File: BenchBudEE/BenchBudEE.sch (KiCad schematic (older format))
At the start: 0 parts

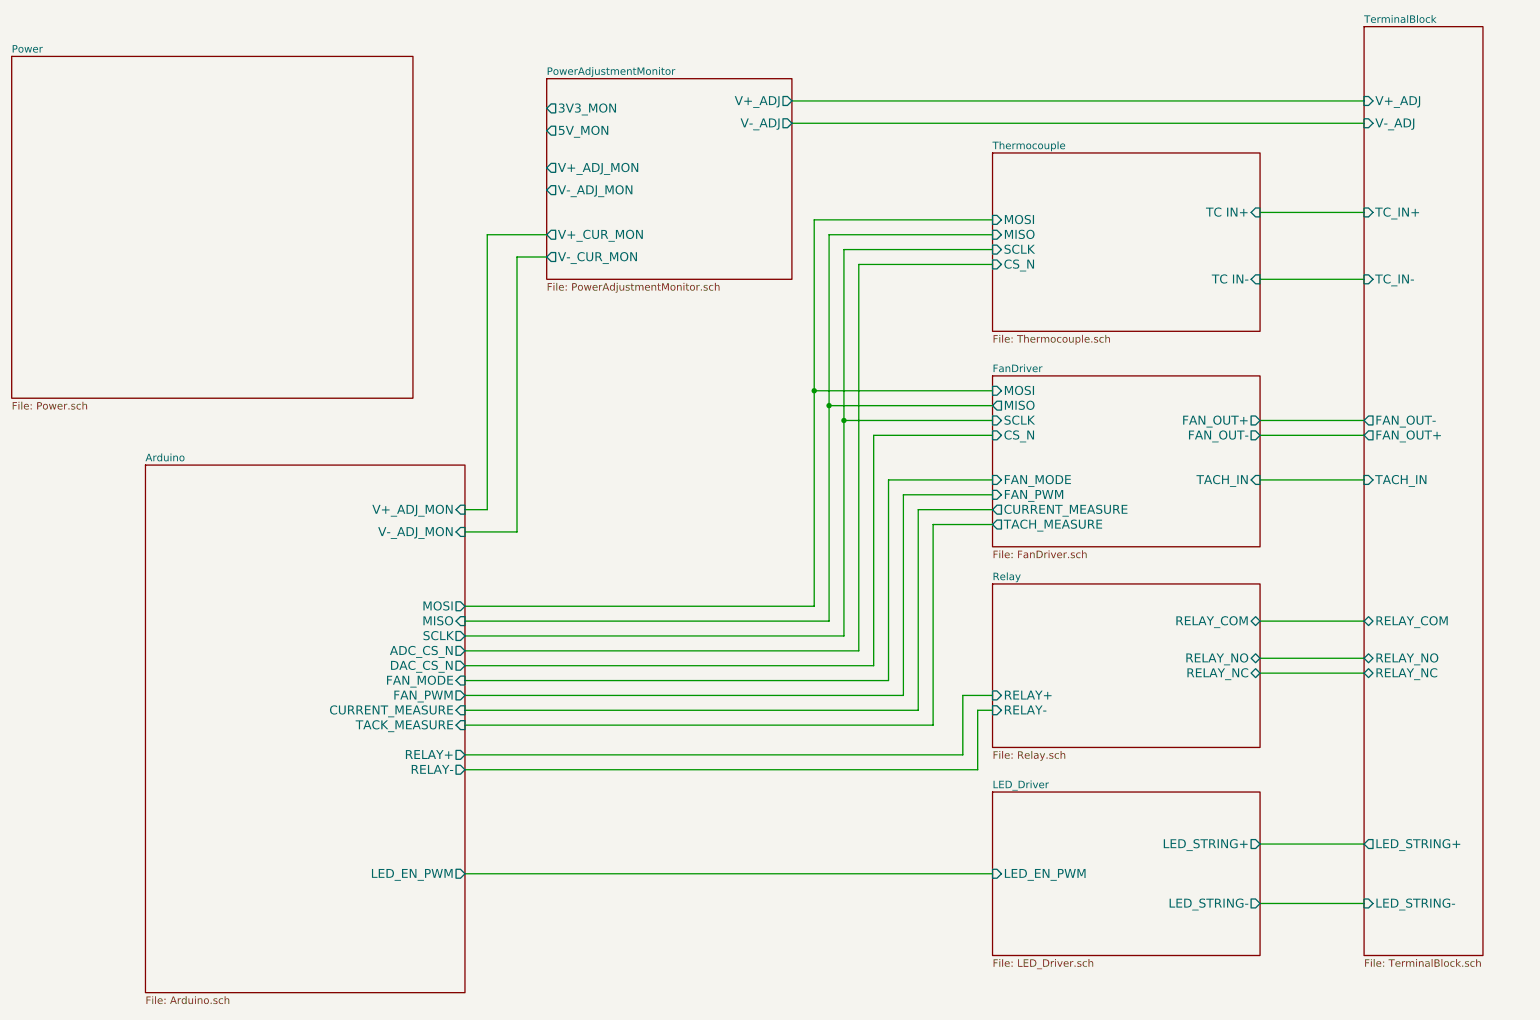
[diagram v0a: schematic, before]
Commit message: Arduino module associated + roughly placed.
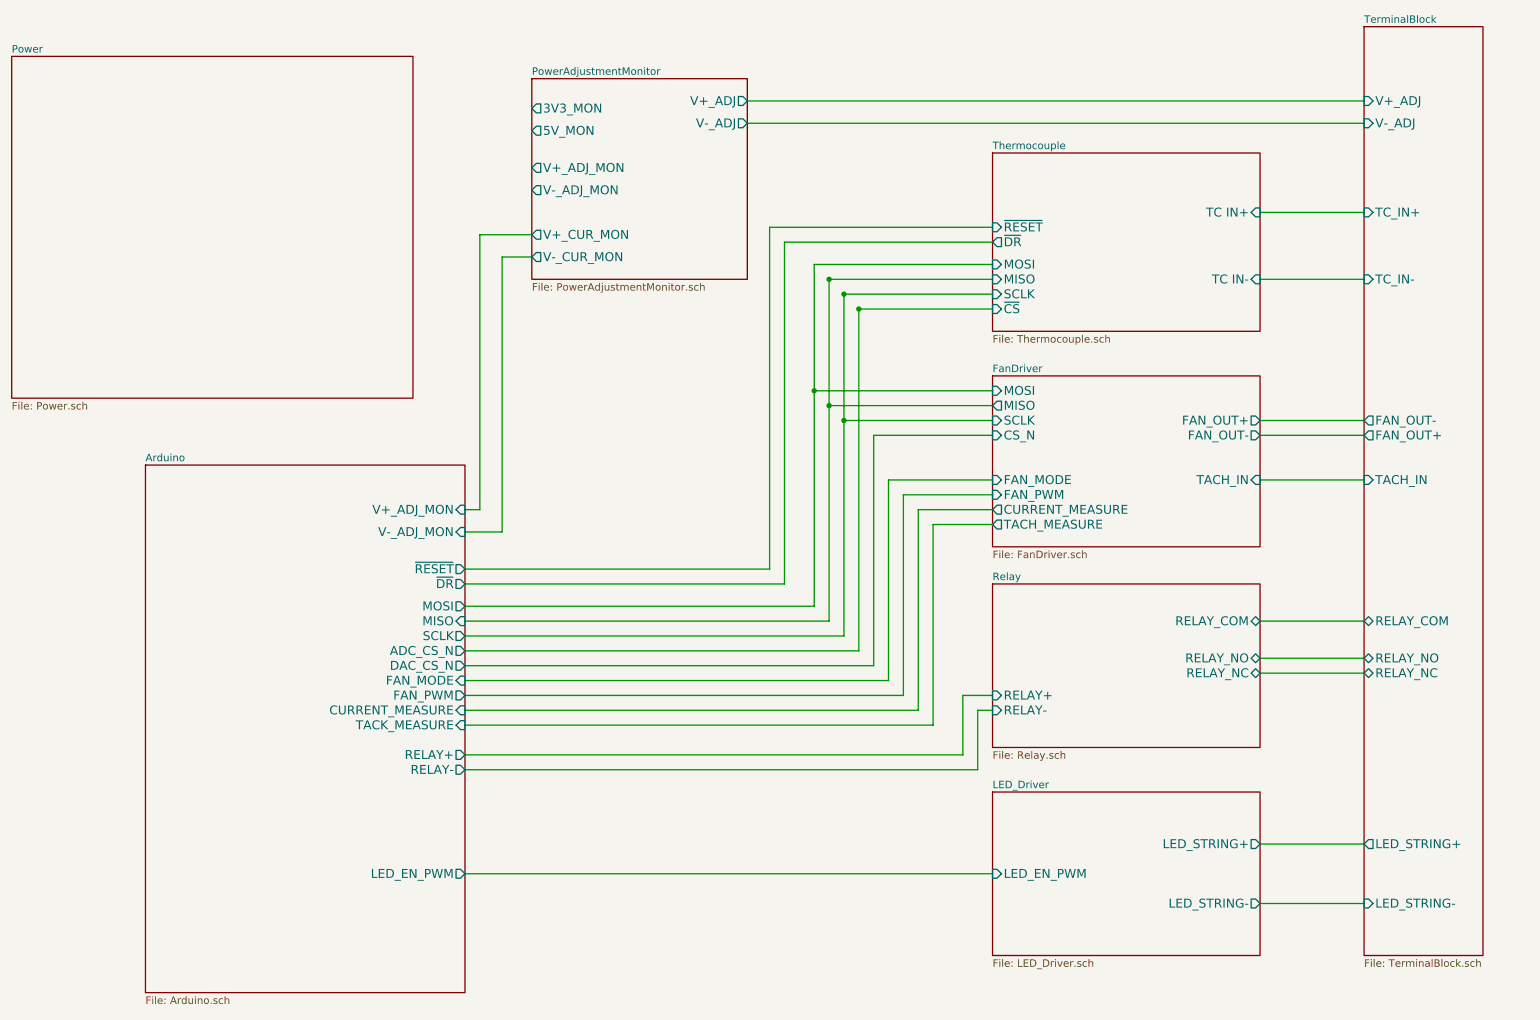
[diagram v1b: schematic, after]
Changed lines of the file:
@@
 Sheet 1 9
 Title ""
-Date "20 feb 2014"
+Date "23 feb 2014"
 Rev ""
 Comp ""
@@
 F2 "TC IN+" I R 9250 1900 60
 F3 "TC IN-" I R 9250 2350 60
-F4 "MISO" I L 7450 2050 60
-F5 "MOSI" I L 7450 1950 60
-F6 "SCLK" I L 7450 2150 60
-F7 "CS_N" I L 7450 2250 60
-$EndSheet
-$Sheet
-S 4450 1000 1650 1350
+F4 "MISO" I L 7450 2350 60
+F5 "MOSI" I L 7450 2250 60
+F6 "SCLK" I L 7450 2450 60
+F7 "~CS" I L 7450 2550 60
+F8 "~DR" O L 7450 2100 60
+F9 "~RESET" I L 7450 2000 60
+$EndSheet
+$Sheet
+S 4350 1000 1450 1350
 U 52F2C572
 F0 "PowerAdjustmentMonitor" 50
 F1 "PowerAdjustmentMonitor.sch" 50
-F2 "V+_ADJ" O R 6100 1150 60
-F3 "V-_ADJ" O R 6100 1300 60
-F4 "3V3_MON" O L 4450 1200 60
-F5 "5V_MON" O L 4450 1350 60
-F6 "V+_ADJ_MON" O L 4450 1600 60
-F7 "V-_ADJ_MON" O L 4450 1750 60
-F8 "V+_CUR_MON" O L 4450 2050 60
-F9 "V-_CUR_MON" O L 4450 2200 60
-$EndSheet
-Wire Wire Line
-	6100 1300 9950 1300
-Wire Wire Line
-	6100 1150 9950 1150
-Wire Wire Line
-	9250 3300 9950 3300
-Wire Wire Line
-	9950 3400 9250 3400
-Wire Wire Line
-	9250 3700 9950 3700
-Wire Wire Line
-	9250 2350 9950 2350
-Wire Wire Line
-	9950 1900 9250 1900
-Wire Wire Line
-	9250 5000 9950 5000
-Wire Wire Line
-	9950 4900 9250 4900
-Wire Wire Line
-	9250 4650 9950 4650
-Wire Wire Line
-	9250 6150 9950 6150
-Wire Wire Line
-	9250 6550 9950 6550
-Wire Wire Line
-	3900 3900 4050 3900
-Wire Wire Line
-	4050 3900 4050 2050
-Wire Wire Line
-	4050 2050 4450 2050
-Wire Wire Line
-	4450 2200 4250 2200
-Wire Wire Line
-	4250 2200 4250 4050
-Wire Wire Line
-	4250 4050 3900 4050
-Wire Wire Line
-	6250 1950 6250 4550
-Wire Wire Line
-	6250 1950 7450 1950
-Wire Wire Line
-	6350 2050 6350 4650
-Wire Wire Line
-	6450 2150 6450 4750
-Wire Wire Line
-	6550 2250 6550 4850
-Wire Wire Line
-	7450 3100 6250 3100
-Connection ~ 6250 3100
-Wire Wire Line
-	7450 3200 6350 3200
-Connection ~ 6350 3200
-Wire Wire Line
-	7450 3300 6450 3300
-Connection ~ 6450 3300
-Wire Wire Line
-	6950 5250 6950 3900
-Wire Wire Line
-	6950 3900 7450 3900
-Wire Wire Line
-	7450 4000 7050 4000
-Wire Wire Line
-	7050 4000 7050 5350
-Wire Wire Line
-	7450 3400 6650 3400
-Wire Wire Line
-	6650 3400 6650 4950
-Wire Wire Line
-	6550 4850 3900 4850
-Wire Wire Line
-	6650 4950 3900 4950
-Wire Wire Line
-	6250 4550 3900 4550
-Wire Wire Line
-	7450 2050 6350 2050
-Wire Wire Line
-	6450 2150 7450 2150
-Wire Wire Line
-	7450 2250 6550 2250
-Wire Wire Line
-	6350 4650 3900 4650
-Wire Wire Line
-	6450 4750 3900 4750
-Wire Wire Line
-	7450 3800 6850 3800
-Wire Wire Line
-	6850 3800 6850 5150
-Wire Wire Line
-	6850 5150 3900 5150
-Wire Wire Line
-	6950 5250 3900 5250
-Wire Wire Line
-	7050 5350 3900 5350
+F2 "V+_ADJ" O R 5800 1150 60
+F3 "V-_ADJ" O R 5800 1300 60
+F4 "3V3_MON" O L 4350 1200 60
+F5 "5V_MON" O L 4350 1350 60
+F6 "V+_ADJ_MON" O L 4350 1600 60
+F7 "V-_ADJ_MON" O L 4350 1750 60
+F8 "V+_CUR_MON" O L 4350 2050 60
+F9 "V-_CUR_MON" O L 4350 2200 60
+$EndSheet
 $Sheet
 S 1750 3600 2150 3550
@@
 F14 "FAN_PWM" O R 3900 5150 60
 F15 "FAN_MODE" I R 3900 5050 60
-$EndSheet
+F16 "~DR" O R 3900 4400 60
+F17 "~RESET" O R 3900 4300 60
+$EndSheet
+Wire Wire Line
+	6750 3700 7450 3700
+Wire Wire Line
+	6750 5050 6750 3700
+Wire Wire Line
+	3900 5050 6750 5050
+Wire Wire Line
+	3900 6350 7450 6350
+Wire Wire Line
+	7350 5650 3900 5650
+Wire Wire Line
+	7350 5250 7350 5650
+Wire Wire Line
+	7450 5250 7350 5250
+Wire Wire Line
+	7250 5150 7450 5150
+Wire Wire Line
+	7250 5550 7250 5150
 Wire Wire Line
 	3900 5550 7250 5550
 Wire Wire Line
-	7250 5550 7250 5150
-Wire Wire Line
-	7250 5150 7450 5150
-Wire Wire Line
-	7450 5250 7350 5250
-Wire Wire Line
-	7350 5250 7350 5650
-Wire Wire Line
-	7350 5650 3900 5650
-Wire Wire Line
-	3900 6350 7450 6350
-Wire Wire Line
-	3900 5050 6750 5050
-Wire Wire Line
-	6750 5050 6750 3700
-Wire Wire Line
-	6750 3700 7450 3700
+	7050 5350 3900 5350
+Wire Wire Line
+	6950 5250 3900 5250
+Wire Wire Line
+	6850 5150 3900 5150
+Wire Wire Line
+	6850 3800 6850 5150
+Wire Wire Line
+	7450 3800 6850 3800
+Wire Wire Line
+	6450 4750 3900 4750
+Wire Wire Line
+	6350 4650 3900 4650
+Wire Wire Line
+	6250 4550 3900 4550
+Wire Wire Line
+	6650 4950 3900 4950
+Wire Wire Line
+	6550 4850 3900 4850
+Wire Wire Line
+	6650 3400 6650 4950
+Wire Wire Line
+	7450 3400 6650 3400
+Wire Wire Line
+	7050 4000 7050 5350
+Wire Wire Line
+	7450 4000 7050 4000
+Wire Wire Line
+	6950 3900 7450 3900
+Wire Wire Line
+	6950 5250 6950 3900
+Connection ~ 6450 3300
+Wire Wire Line
+	7450 3300 6450 3300
+Connection ~ 6350 3200
+Wire Wire Line
+	7450 3200 6350 3200
+Connection ~ 6250 3100
+Wire Wire Line
+	7450 3100 6250 3100
+Wire Wire Line
+	6250 2250 6250 4550
+Wire Wire Line
+	4150 4050 3900 4050
+Wire Wire Line
+	4150 2200 4150 4050
+Wire Wire Line
+	4350 2200 4150 2200
+Wire Wire Line
+	4000 2050 4350 2050
+Wire Wire Line
+	4000 3900 4000 2050
+Wire Wire Line
+	3900 3900 4000 3900
+Wire Wire Line
+	9250 6550 9950 6550
+Wire Wire Line
+	9250 6150 9950 6150
+Wire Wire Line
+	9250 4650 9950 4650
+Wire Wire Line
+	9950 4900 9250 4900
+Wire Wire Line
+	9250 5000 9950 5000
+Wire Wire Line
+	9950 1900 9250 1900
+Wire Wire Line
+	9250 2350 9950 2350
+Wire Wire Line
+	9250 3700 9950 3700
+Wire Wire Line
+	9950 3400 9250 3400
+Wire Wire Line
+	9250 3300 9950 3300
+Wire Wire Line
+	5800 1150 9950 1150
+Wire Wire Line
+	5800 1300 9950 1300
+Wire Wire Line
+	7450 2550 6550 2550
+Connection ~ 6550 2550
+Wire Wire Line
+	6550 2550 6550 4850
+Wire Wire Line
+	7450 2450 6450 2450
+Connection ~ 6450 2450
+Wire Wire Line
+	6450 2450 6450 4750
+Wire Wire Line
+	7450 2350 6350 2350
+Connection ~ 6350 2350
+Wire Wire Line
+	6350 2350 6350 4650
+Wire Wire Line
+	6250 2250 7450 2250
+Wire Wire Line
+	7450 2100 6050 2100
+Wire Wire Line
+	6050 2100 6050 4400
+Wire Wire Line
+	6050 4400 3900 4400
+Wire Wire Line
+	3900 4300 5950 4300
+Wire Wire Line
+	5950 4300 5950 2000
+Wire Wire Line
+	5950 2000 7450 2000
 $EndSCHEMATC

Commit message: Fan/Current driver associated + roughly placed.
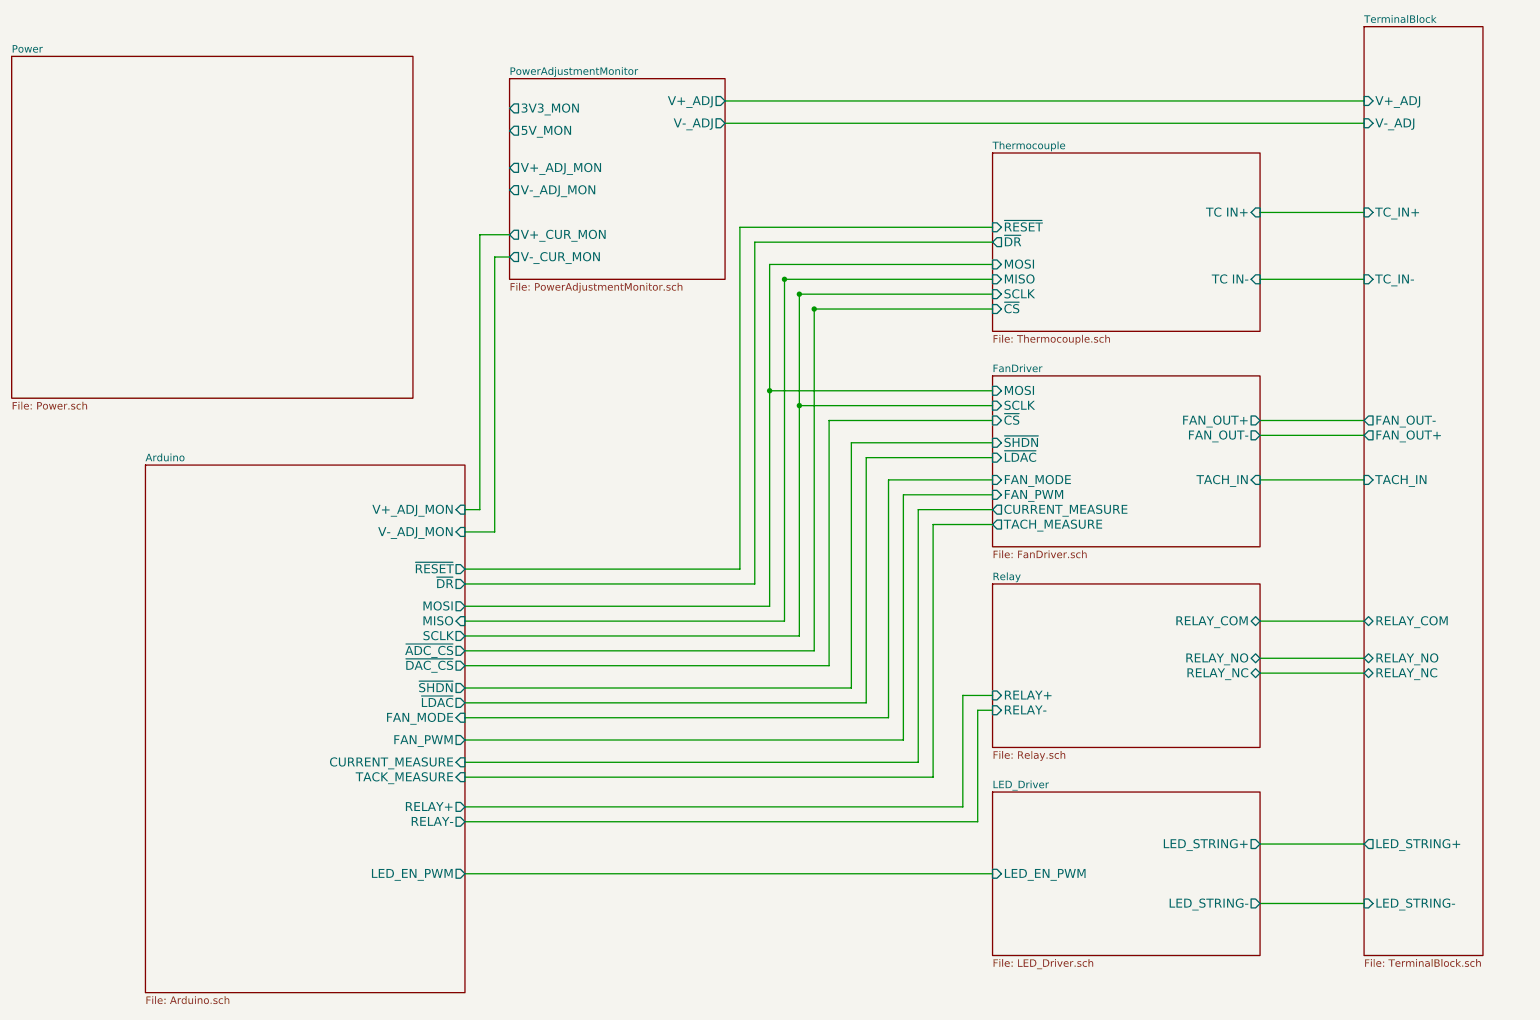
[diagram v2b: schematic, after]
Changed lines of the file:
@@
-$EndSheet
-$Sheet
-S 7450 3000 1800 1150
-U 52F1416D
-F0 "FanDriver" 50
-F1 "FanDriver.sch" 50
-F2 "CURRENT_MEASURE" O L 7450 3900 60
-F3 "MOSI" I L 7450 3100 60
-F4 "MISO" O L 7450 3200 60
-F5 "SCLK" I L 7450 3300 60
-F6 "CS_N" I L 7450 3400 60
-F7 "TACH_IN" I R 9250 3700 60
-F8 "TACH_MEASURE" O L 7450 4000 60
-F9 "FAN_OUT+" O R 9250 3300 60
-F10 "FAN_OUT-" O R 9250 3400 60
-F11 "FAN_MODE" I L 7450 3700 60
-F12 "FAN_PWM" I L 7450 3800 60
 $EndSheet
 $Sheet
@@
 $EndSheet
 $Sheet
-S 4350 1000 1450 1350
+S 4200 1000 1450 1350
 U 52F2C572
 F0 "PowerAdjustmentMonitor" 50
 F1 "PowerAdjustmentMonitor.sch" 50
-F2 "V+_ADJ" O R 5800 1150 60
-F3 "V-_ADJ" O R 5800 1300 60
-F4 "3V3_MON" O L 4350 1200 60
-F5 "5V_MON" O L 4350 1350 60
-F6 "V+_ADJ_MON" O L 4350 1600 60
-F7 "V-_ADJ_MON" O L 4350 1750 60
-F8 "V+_CUR_MON" O L 4350 2050 60
-F9 "V-_CUR_MON" O L 4350 2200 60
+F2 "V+_ADJ" O R 5650 1150 60
+F3 "V-_ADJ" O R 5650 1300 60
+F4 "3V3_MON" O L 4200 1200 60
+F5 "5V_MON" O L 4200 1350 60
+F6 "V+_ADJ_MON" O L 4200 1600 60
+F7 "V-_ADJ_MON" O L 4200 1750 60
+F8 "V+_CUR_MON" O L 4200 2050 60
+F9 "V-_CUR_MON" O L 4200 2200 60
 $EndSheet
 $Sheet
@@
 F3 "MISO" I R 3900 4650 60
 F4 "SCLK" O R 3900 4750 60
-F5 "TACK_MEASURE" I R 3900 5350 60
-F6 "RELAY+" O R 3900 5550 60
-F7 "RELAY-" O R 3900 5650 60
+F5 "TACK_MEASURE" I R 3900 5700 60
+F6 "RELAY+" O R 3900 5900 60
+F7 "RELAY-" O R 3900 6000 60
 F8 "LED_EN_PWM" O R 3900 6350 60
-F9 "CURRENT_MEASURE" I R 3900 5250 60
+F9 "CURRENT_MEASURE" I R 3900 5600 60
 F10 "V+_ADJ_MON" I R 3900 3900 60
 F11 "V-_ADJ_MON" I R 3900 4050 60
-F12 "DAC_CS_N" O R 3900 4950 60
-F13 "ADC_CS_N" O R 3900 4850 60
-F14 "FAN_PWM" O R 3900 5150 60
-F15 "FAN_MODE" I R 3900 5050 60
-F16 "~DR" O R 3900 4400 60
-F17 "~RESET" O R 3900 4300 60
+F12 "FAN_PWM" O R 3900 5450 60
+F13 "FAN_MODE" I R 3900 5300 60
+F14 "~DR" O R 3900 4400 60
+F15 "~RESET" O R 3900 4300 60
+F16 "~LDAC" O R 3900 5200 60
+F17 "~SHDN" O R 3900 5100 60
+F18 "~ADC_CS" O R 3900 4850 60
+F19 "~DAC_CS" O R 3900 4950 60
 $EndSheet
 Wire Wire Line
 	6750 3700 7450 3700
 Wire Wire Line
-	6750 5050 6750 3700
-Wire Wire Line
-	3900 5050 6750 5050
+	6750 5300 6750 3700
+Wire Wire Line
+	3900 5300 6750 5300
 Wire Wire Line
 	3900 6350 7450 6350
 Wire Wire Line
-	7350 5650 3900 5650
-Wire Wire Line
-	7350 5250 7350 5650
+	7350 6000 3900 6000
+Wire Wire Line
+	7350 5250 7350 6000
 Wire Wire Line
 	7450 5250 7350 5250
@@
 	7250 5150 7450 5150
 Wire Wire Line
-	7250 5550 7250 5150
-Wire Wire Line
-	3900 5550 7250 5550
-Wire Wire Line
-	7050 5350 3900 5350
-Wire Wire Line
-	6950 5250 3900 5250
-Wire Wire Line
-	6850 5150 3900 5150
-Wire Wire Line
-	6850 3800 6850 5150
+	7250 5900 7250 5150
+Wire Wire Line
+	3900 5900 7250 5900
+Wire Wire Line
+	7050 5700 3900 5700
+Wire Wire Line
+	6950 5600 3900 5600
+Wire Wire Line
+	6850 5450 3900 5450
+Wire Wire Line
+	6850 3800 6850 5450
 Wire Wire Line
 	7450 3800 6850 3800
 Wire Wire Line
-	6450 4750 3900 4750
-Wire Wire Line
-	6350 4650 3900 4650
-Wire Wire Line
-	6250 4550 3900 4550
-Wire Wire Line
-	6650 4950 3900 4950
-Wire Wire Line
-	6550 4850 3900 4850
-Wire Wire Line
-	6650 3400 6650 4950
-Wire Wire Line
-	7450 3400 6650 3400
-Wire Wire Line
-	7050 4000 7050 5350
+	6150 4750 3900 4750
+Wire Wire Line
+	6050 4650 3900 4650
+Wire Wire Line
+	5950 4550 3900 4550
+Wire Wire Line
+	6350 4950 3900 4950
+Wire Wire Line
+	6250 4850 3900 4850
+Wire Wire Line
+	6350 3300 6350 4950
+Wire Wire Line
+	7050 4000 7050 5700
 Wire Wire Line
 	7450 4000 7050 4000
@@
 	6950 3900 7450 3900
 Wire Wire Line
-	6950 5250 6950 3900
-Connection ~ 6450 3300
-Wire Wire Line
-	7450 3300 6450 3300
-Connection ~ 6350 3200
-Wire Wire Line
-	7450 3200 6350 3200
-Connection ~ 6250 3100
-Wire Wire Line
-	7450 3100 6250 3100
-Wire Wire Line
-	6250 2250 6250 4550
-Wire Wire Line
-	4150 4050 3900 4050
-Wire Wire Line
-	4150 2200 4150 4050
-Wire Wire Line
-	4350 2200 4150 2200
-Wire Wire Line
-	4000 2050 4350 2050
+	6950 5600 6950 3900
+Wire Wire Line
+	5950 2250 5950 4550
+Wire Wire Line
+	4100 4050 3900 4050
+Wire Wire Line
+	4100 2200 4100 4050
+Wire Wire Line
+	4200 2200 4100 2200
+Wire Wire Line
+	4000 2050 4200 2050
 Wire Wire Line
 	4000 3900 4000 2050
@@
 	9250 3300 9950 3300
 Wire Wire Line
-	5800 1150 9950 1150
-Wire Wire Line
-	5800 1300 9950 1300
-Wire Wire Line
-	7450 2550 6550 2550
-Connection ~ 6550 2550
-Wire Wire Line
-	6550 2550 6550 4850
-Wire Wire Line
-	7450 2450 6450 2450
-Connection ~ 6450 2450
-Wire Wire Line
-	6450 2450 6450 4750
-Wire Wire Line
-	7450 2350 6350 2350
-Connection ~ 6350 2350
-Wire Wire Line
-	6350 2350 6350 4650
-Wire Wire Line
-	6250 2250 7450 2250
-Wire Wire Line
-	7450 2100 6050 2100
-Wire Wire Line
-	6050 2100 6050 4400
-Wire Wire Line
-	6050 4400 3900 4400
-Wire Wire Line
-	3900 4300 5950 4300
-Wire Wire Line
-	5950 4300 5950 2000
-Wire Wire Line
-	5950 2000 7450 2000
+	5650 1150 9950 1150
+Wire Wire Line
+	5650 1300 9950 1300
+Wire Wire Line
+	7450 2550 6250 2550
+Connection ~ 6250 2550
+Wire Wire Line
+	6250 2550 6250 4850
+Wire Wire Line
+	6150 2450 7450 2450
+Connection ~ 6150 2450
+Wire Wire Line
+	6150 2450 6150 4750
+Wire Wire Line
+	7450 2350 6050 2350
+Connection ~ 6050 2350
+Wire Wire Line
+	6050 2350 6050 4650
+Wire Wire Line
+	5950 2250 7450 2250
+Wire Wire Line
+	7450 2100 5850 2100
+Wire Wire Line
+	5850 2100 5850 4400
+Wire Wire Line
+	5850 4400 3900 4400
+Wire Wire Line
+	3900 4300 5750 4300
+Wire Wire Line
+	5750 4300 5750 2000
+Wire Wire Line
+	5750 2000 7450 2000
+Wire Wire Line
+	7450 3100 5950 3100
+Connection ~ 5950 3100
+Wire Wire Line
+	7450 3200 6150 3200
+Connection ~ 6150 3200
+Wire Wire Line
+	6350 3300 7450 3300
+$Sheet
+S 7450 3000 1800 1150
+U 52F1416D
+F0 "FanDriver" 50
+F1 "FanDriver.sch" 50
+F2 "CURRENT_MEASURE" O L 7450 3900 60
+F3 "SCLK" I L 7450 3200 60
+F4 "TACH_IN" I R 9250 3700 60
+F5 "TACH_MEASURE" O L 7450 4000 60
+F6 "FAN_OUT+" O R 9250 3300 60
+F7 "FAN_OUT-" O R 9250 3400 60
+F8 "FAN_MODE" I L 7450 3700 60
+F9 "FAN_PWM" I L 7450 3800 60
+F10 "~CS" I L 7450 3300 60
+F11 "MOSI" I L 7450 3100 60
+F12 "~LDAC" I L 7450 3550 60
+F13 "~SHDN" I L 7450 3450 60
+$EndSheet
+Wire Wire Line
+	3900 5100 6500 5100
+Wire Wire Line
+	6500 5100 6500 3450
+Wire Wire Line
+	6500 3450 7450 3450
+Wire Wire Line
+	7450 3550 6600 3550
+Wire Wire Line
+	6600 3550 6600 5200
+Wire Wire Line
+	6600 5200 3900 5200
 $EndSCHEMATC
